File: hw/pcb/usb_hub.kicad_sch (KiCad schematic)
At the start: 13 parts, among them U4 USB2422, Y1 24MHz

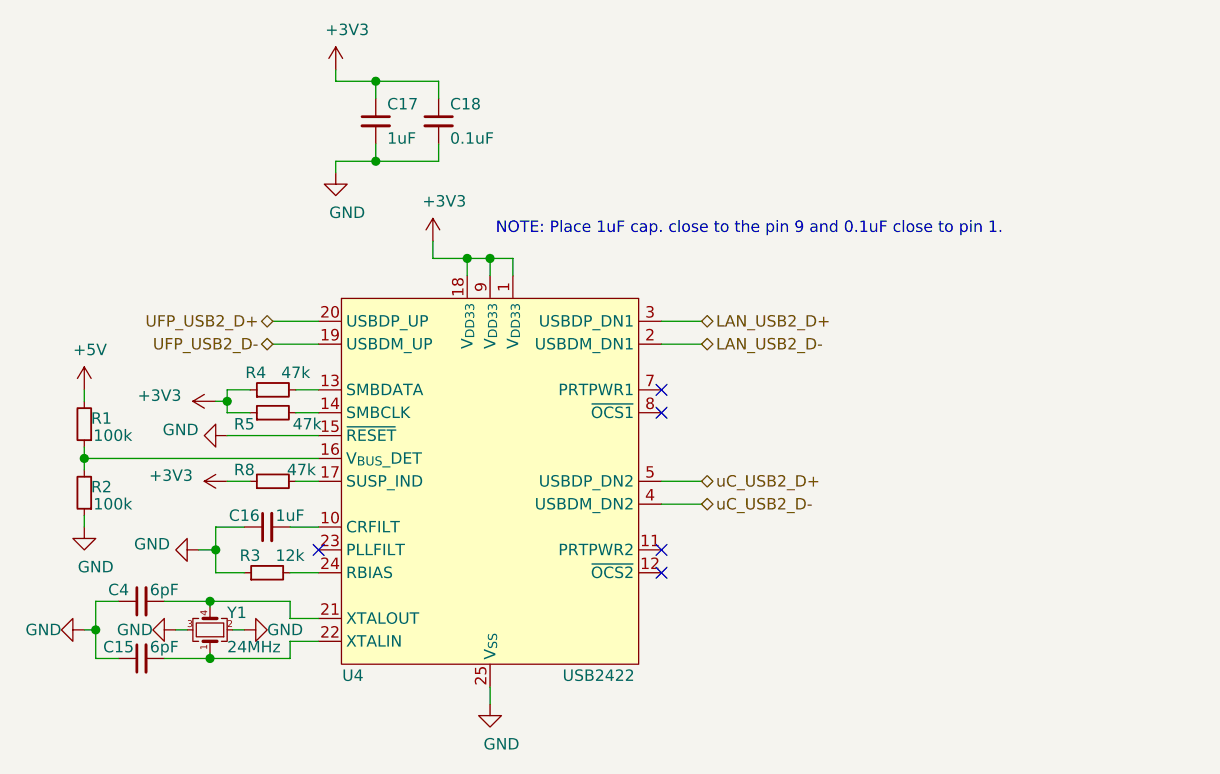
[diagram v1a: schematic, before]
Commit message: whisperbounce: pcb v1
Includes schematic and assigment tweaks

Signed-off-by: Dominik Sliwa <dominik@sliwa.io>
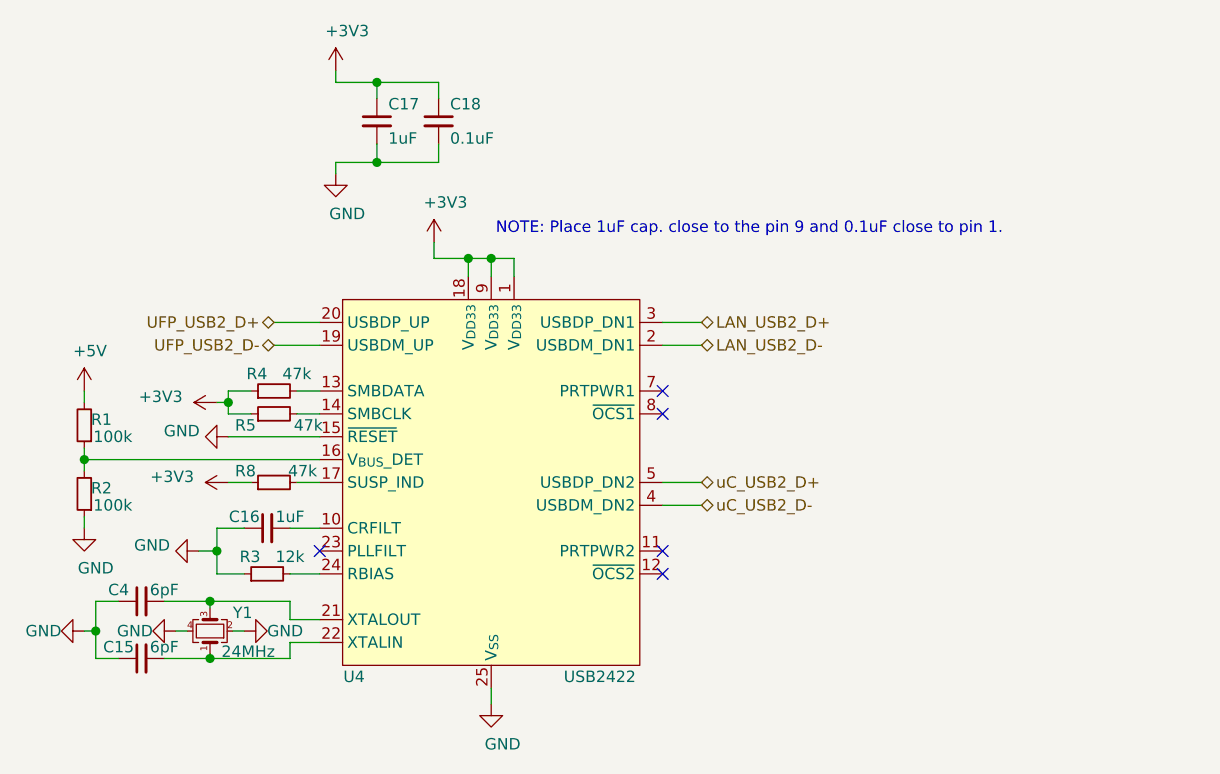
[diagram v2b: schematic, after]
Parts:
- removed Y1: 24MHz, Oscillator:Oscillator_SMD_Abracon_ASCO-4Pin_1.6x1.2mm, symbol Device:Crystal_GND23_Small
- added Y1: 24MHz, Oscillator:Oscillator_SMD_Abracon_ASCO-4Pin_1.6x1.2mm, symbol Device:Crystal_GND24_Small
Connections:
- net GND: now also Y1.2, Y1.4
- net at C4.2, U4.21 (XTALOUT): now also Y1.3
- net at C15.2, U4.22 (XTALIN): now also Y1.1
